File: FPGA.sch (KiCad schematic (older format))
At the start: 0 parts

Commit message: Add FPGA schematic and set up decoupling capacitors
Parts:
- added C?: 330u, symbol Device:C
- added C? (x8): 4.7u, symbol Device:C
- added C? (x13): 0.47u, symbol Device:C
- added C?: 100u, symbol Device:C
- added C?: 47u, symbol Device:C
- added U? (x4): XC7A100T-FTG256, symbol FPGA_Xilinx_Artix7:XC7A100T-FTG256
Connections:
- new net +1V0: C?.1, C?.1, C?.1, C?.1, C?.1, C?.1, C?.1, C?.1, C?.1, C?.1, C?.1, C?.1, C?.1, C?.1, C?.1, C?.1, C?.1, C?.1, U?.E10 (VCCBRAM), U?.F11 (VCCBRAM), U?.F7 (VCCINT), U?.F9 (VCCINT), U?.G6 (VCCINT), U?.H9 (VCCINT), U?.J6 (VCCINT), U?.K9 (VCCINT), U?.L8 (VCCINT)
- new net +1V8: C?.1, C?.1, C?.1, C?.1, C?.1, C?.1, U?.G10 (VCCAUX), U?.J10 (VCCAUX), U?.K11 (VCCAUX), U?.L10 (VCCAUX)
- new net GND: C?.2, C?.2, C?.2, C?.2, C?.2, C?.2, C?.2, C?.2, C?.2, C?.2, C?.2, C?.2, C?.2, C?.2, C?.2, C?.2, C?.2, C?.2, C?.2, C?.2, C?.2, C?.2, C?.2, C?.2, U?.A1 (GND), U?.A11 (GND), U?.B8 (GND), U?.C15 (GND), U?.C5 (GND), U?.D12 (GND), U?.D2 (GND), U?.E9 (GND), U?.F10 (GND), U?.F16 (GND), U?.F6 (GND), U?.G13 (GND), U?.G3 (GND), U?.G9 (GND), U?.H6 (GND), U?.J11 (GND), U?.J9 (GND), U?.K14 (GND), U?.K4 (GND), U?.K6 (GND), U?.L1 (GND), U?.L11 (GND), U?.M8 (GND), U?.N15 (GND), U?.N5 (GND), U?.P12 (GND), U?.P2 (GND), U?.R9 (GND), U?.T16 (GND), U?.T6 (GND)

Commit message: Set up FPGA power and enable I/O banks
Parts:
- removed U?: XC7A100T-FTG256, symbol FPGA_Xilinx_Artix7:XC7A100T-FTG256
- added C? (x2): 47u, symbol Device:C
- added C? (x2): 4.7u, symbol Device:C
- added C? (x4): 0.47u, symbol Device:C
- added U?: XC7A100T-FTG256, symbol FPGA_Xilinx_Artix7:XC7A100T-FTG256
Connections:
- net +1V8: now also U?.G8 (VCCADC_0)
- net GND: now also U?.A16 (VCCO_15), U?.B13 (VCCO_15), U?.C10 (VCCO_15), U?.E14 (VCCO_15), U?.F8 (VCCBATT_0), U?.G7 (GNDADC_0), U?.H15 (VCCO_15), U?.J12 (VCCO_15), C?.2, C?.2, C?.2, C?.2, C?.2, C?.2, C?.2, C?.2, U?.A6 (VCCO_35), U?.B3 (VCCO_35), U?.D7 (VCCO_35), U?.E4 (VCCO_35), U?.F1 (VCCO_35), U?.J2 (VCCO_35), U?.M3 (VCCO_34), U?.R4 (VCCO_34), U?.T1 (VCCO_34)
- net +3V3: now reaches U?.L16 (VCCO_14)
- net +3V3: now also U?.L6 (VCCO_0), U?.M13 (VCCO_14), U?.N10 (VCCO_14), U?.P7 (VCCO_14), U?.R14 (VCCO_14), U?.T11 (VCCO_14), C?.1, C?.1, C?.1, C?.1, C?.1, C?.1, C?.1, C?.1
- no-connect marks 0 -> 120
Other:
- moved on the sheet: C?, U?A, U?C, U?D

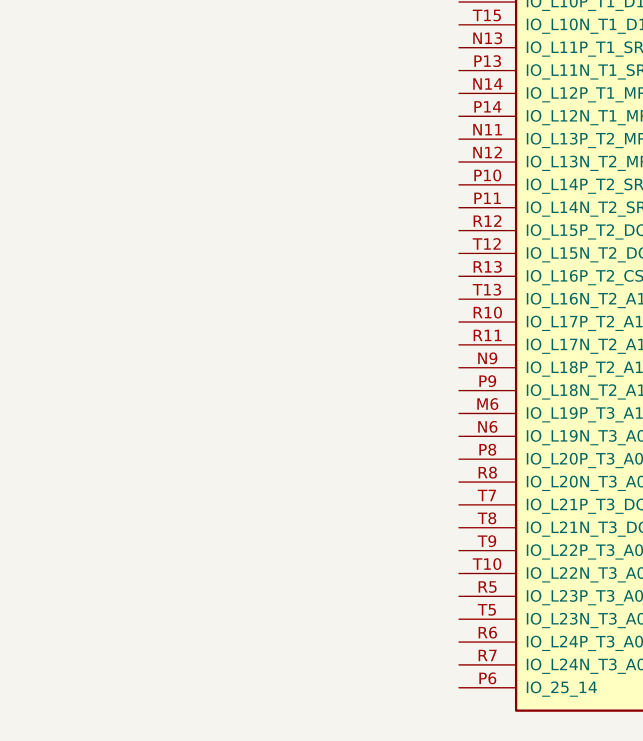
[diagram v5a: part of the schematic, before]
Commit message: Add oscillator
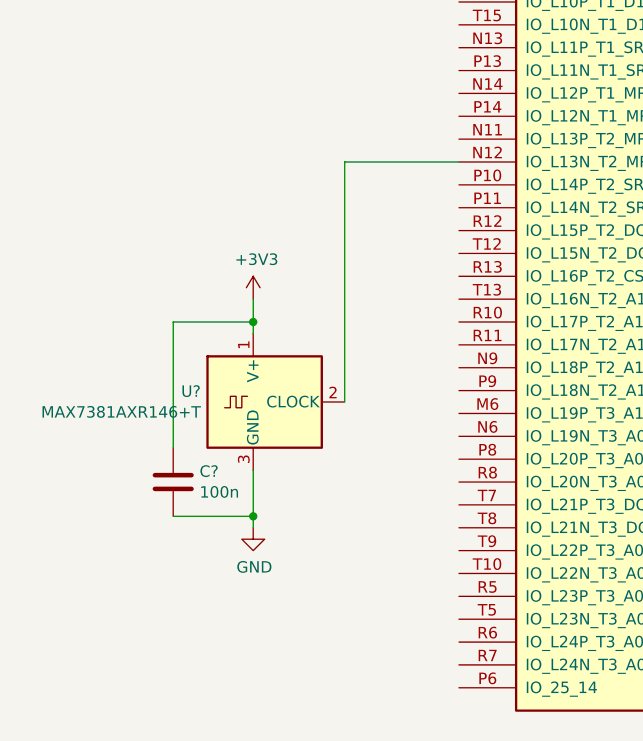
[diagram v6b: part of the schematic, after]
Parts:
- added C?: 100n, symbol Device:C
- added U?: MAX7381AXR146+T, Package_TO_SOT_SMD:SOT-323_SC-70, symbol Oscillator:MAX7375AXR805
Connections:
- net +3V3: now also C?.2, U?.1 (V+)
- net GND: now also C?.1, U?.3 (GND)
- net at U?.N12 (IO_L13N_T2_MRCC_14): now also U?.2 (CLOCK)
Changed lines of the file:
@@
 	1400 9750 1500 9750
 Connection ~ 1500 9750
+$Comp
+L Oscillator:MAX7375AXR805 U?
+U 1 1 5E016B02
+P 700 5450
+F 0 "U?" H 471 5496 50  0000 R CNN
+F 1 "MAX7381AXR146+T" H 471 5405 50  0000 R CNN
+F 2 "Package_TO_SOT_SMD:SOT-323_SC-70" H 1800 5100 50  0001 C CNN
+F 3 "https://datasheets.maximintegrated.com/en/ds/MAX7375.pdf" H 600 5450 50  0001 C CNN
+	1    700  5450
+	1    0    0    -1
+$EndComp
+$Comp
+L power:+3V3 #PWR?
+U 1 1 5E0228B1
+P 700 5000
+F 0 "#PWR?" H 700 4850 50  0001 C CNN
+F 1 "+3V3" H 715 5173 50  0000 C CNN
+F 2 "" H 700 5000 50  0001 C CNN
+F 3 "" H 700 5000 50  0001 C CNN
+	1    700  5000
+	1    0    0    -1
+$EndComp
+$Comp
+L power:GND #PWR?
+U 1 1 5E0231C4
+P 700 6000
+F 0 "#PWR?" H 700 5750 50  0001 C CNN
+F 1 "GND" H 705 5827 50  0000 C CNN
+F 2 "" H 700 6000 50  0001 C CNN
+F 3 "" H 700 6000 50  0001 C CNN
+	1    700  6000
+	1    0    0    -1
+$EndComp
+Wire Wire Line
+	700  5750 700  5950
+Wire Wire Line
+	700  5150 700  5100
+$Comp
+L Device:C C?
+U 1 1 5E031A74
+P 350 5800
+F 0 "C?" H 235 5754 50  0000 R CNN
+F 1 "100n" H 235 5845 50  0000 R CNN
+F 2 "" H 388 5650 50  0001 C CNN
+F 3 "~" H 350 5800 50  0001 C CNN
+	1    350  5800
+	-1   0    0    1
+$EndComp
+Wire Wire Line
+	350  5950 700  5950
+Connection ~ 700  5950
+Wire Wire Line
+	700  5950 700  6000
+Wire Wire Line
+	350  5650 350  5100
+Wire Wire Line
+	350  5100 700  5100
+Connection ~ 700  5100
+Wire Wire Line
+	700  5100 700  5000
+Wire Wire Line
+	1100 5450 1100 4400
+Wire Wire Line
+	1100 4400 1600 4400
 $EndSCHEMATC

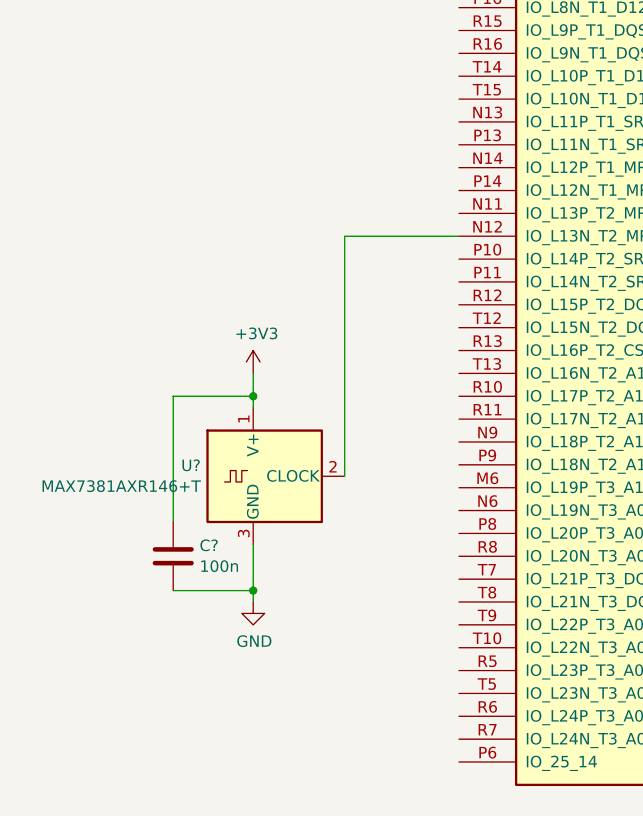
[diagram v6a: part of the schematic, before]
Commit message: Use another oscillator, with a custom symbol
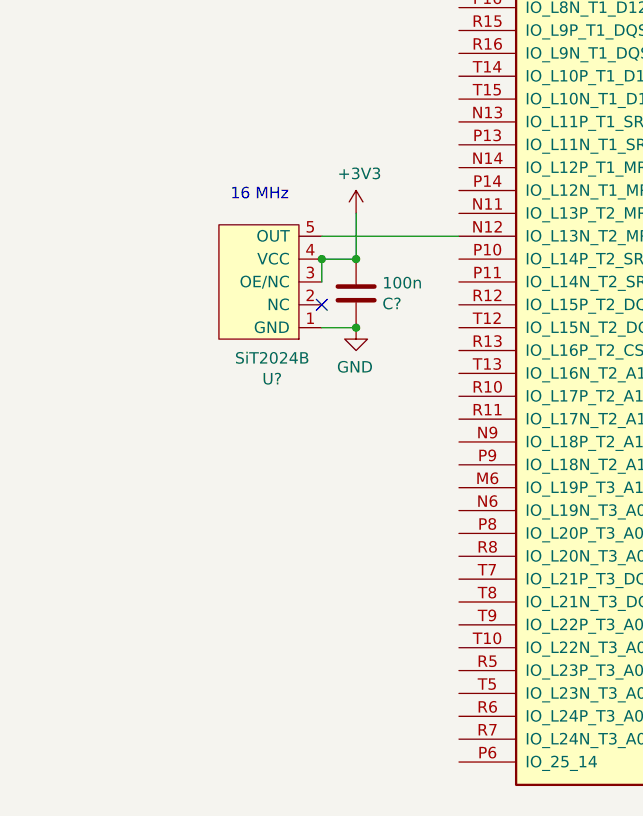
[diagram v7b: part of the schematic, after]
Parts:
- removed C?: 100n, symbol Device:C
- removed U?: MAX7381AXR146+T, Package_TO_SOT_SMD:SOT-323_SC-70, symbol Oscillator:MAX7375AXR805
- added C?: 100n, symbol Device:C
- added U?: SiT2024B, symbol sit-oscillator:SiT2024B
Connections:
- net +3V3: now also C?.2, U?.3 (OE/NC), U?.4 (VCC)
- net GND: now also C?.1, U?.1 (GND)
- net at U?.N12 (IO_L13N_T2_MRCC_14): now also U?.5 (OUT)
- no-connect marks 120 -> 121
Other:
- note added: "16 MHz"
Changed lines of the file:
@@
 Connection ~ 1500 9750
 $Comp
-L Oscillator:MAX7375AXR805 U?
-U 1 1 5E016B02
-P 700 5450
-F 0 "U?" H 471 5496 50  0000 R CNN
-F 1 "MAX7381AXR146+T" H 471 5405 50  0000 R CNN
-F 2 "Package_TO_SOT_SMD:SOT-323_SC-70" H 1800 5100 50  0001 C CNN
-F 3 "https://datasheets.maximintegrated.com/en/ds/MAX7375.pdf" H 600 5450 50  0001 C CNN
-	1    700  5450
-	1    0    0    -1
+L sit-oscillator:SiT2024B U?
+U 1 1 5E17B373
+P 900 4950
+F 0 "U?" H 783 5025 50  0000 C CNN
+F 1 "SiT2024B" H 783 4934 50  0000 C CNN
+F 2 "" H 700 4900 50  0001 C CNN
+F 3 "" H 700 4900 50  0001 C CNN
+	1    900  4950
+	1    0    0    1
 $EndComp
+Text Notes 600  4250 0    50   ~ 0
+16 MHz
+NoConn ~ 1000 4700
 $Comp
 L power:+3V3 #PWR?
-U 1 1 5E0228B1
-P 700 5000
-F 0 "#PWR?" H 700 4850 50  0001 C CNN
-F 1 "+3V3" H 715 5173 50  0000 C CNN
-F 2 "" H 700 5000 50  0001 C CNN
-F 3 "" H 700 5000 50  0001 C CNN
-	1    700  5000
-	1    0    0    -1
-$EndComp
-$Comp
-L power:GND #PWR?
-U 1 1 5E0231C4
-P 700 6000
-F 0 "#PWR?" H 700 5750 50  0001 C CNN
-F 1 "GND" H 705 5827 50  0000 C CNN
-F 2 "" H 700 6000 50  0001 C CNN
-F 3 "" H 700 6000 50  0001 C CNN
-	1    700  6000
+U 1 1 5E1D3E0A
+P 1150 4300
+F 0 "#PWR?" H 1150 4150 50  0001 C CNN
+F 1 "+3V3" H 1165 4473 50  0000 C CNN
+F 2 "" H 1150 4300 50  0001 C CNN
+F 3 "" H 1150 4300 50  0001 C CNN
+	1    1150 4300
 	1    0    0    -1
 $EndComp
 Wire Wire Line
-	700  5750 700  5950
+	1000 4500 1150 4500
+$Comp
+L power:GND #PWR?
+U 1 1 5E1DBA8B
+P 1150 4800
+F 0 "#PWR?" H 1150 4550 50  0001 C CNN
+F 1 "GND" H 1155 4627 50  0000 C CNN
+F 2 "" H 1150 4800 50  0001 C CNN
+F 3 "" H 1150 4800 50  0001 C CNN
+	1    1150 4800
+	-1   0    0    -1
+$EndComp
 Wire Wire Line
-	700  5150 700  5100
+	1000 4800 1150 4800
+Wire Wire Line
+	1000 4400 1600 4400
+Wire Wire Line
+	1000 4600 1000 4500
+Connection ~ 1000 4500
 $Comp
 L Device:C C?
-U 1 1 5E031A74
-P 350 5800
-F 0 "C?" H 235 5754 50  0000 R CNN
-F 1 "100n" H 235 5845 50  0000 R CNN
-F 2 "" H 388 5650 50  0001 C CNN
-F 3 "~" H 350 5800 50  0001 C CNN
-	1    350  5800
-	-1   0    0    1
+U 1 1 5E245697
+P 1150 4650
+F 0 "C?" H 1265 4696 50  0000 L CNN
+F 1 "100n" H 1265 4605 50  0000 L CNN
+F 2 "" H 1188 4500 50  0001 C CNN
+F 3 "~" H 1150 4650 50  0001 C CNN
+	1    1150 4650
+	1    0    0    1
 $EndComp
 Wire Wire Line
-	350  5950 700  5950
-Connection ~ 700  5950
-Wire Wire Line
-	700  5950 700  6000
-Wire Wire Line
-	350  5650 350  5100
-Wire Wire Line
-	350  5100 700  5100
-Connection ~ 700  5100
-Wire Wire Line
-	700  5100 700  5000
-Wire Wire Line
-	1100 5450 1100 4400
-Wire Wire Line
-	1100 4400 1600 4400
+	1150 4300 1150 4500
+Connection ~ 1150 4500
+Connection ~ 1150 4800
 $EndSCHEMATC
